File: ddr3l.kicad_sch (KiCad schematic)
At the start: 1 part

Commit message: write some things down
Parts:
- U1: renamed from U?; value MCIMX6YxxVMxxxx -> MCIMX6Y2DVM09AB; Manufacturer (none) -> NXP; MfgPartNo (none) -> MCIMX6Y2DVM09AB; Vendor (none) -> Digi-Key; VendorPartNo (none) -> 568-14995-ND
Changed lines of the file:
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@@
   (symbol (lib_id "catfood:MCIMX6YxxVMxxxx") (at 50.8 54.61 0) (unit 3)
     (in_bom yes) (on_board yes) (fields_autoplaced)
-    (property "Reference" "U?" (id 0) (at 50.8 24.13 0))
-    (property "Value" "MCIMX6YxxVMxxxx" (id 1) (at 50.8 26.67 0))
+    (property "Reference" "U1" (id 0) (at 50.8 24.13 0))
+    (property "Value" "MCIMX6Y2DVM09AB" (id 1) (at 50.8 26.67 0))
     (property "Footprint" "" (id 2) (at 40.64 35.56 0)
       (effects (font (size 1.27 1.27)) hide)
@@
       (effects (font (size 1.27 1.27)) hide)
     )
+    (property "Manufacturer" "NXP" (id 4) (at 50.8 34.29 0)
+      (effects (font (size 1.27 1.27)) hide)
+    )
+    (property "MfgPartNo" "MCIMX6Y2DVM09AB" (id 5) (at 50.8 36.83 0)
+      (effects (font (size 1.27 1.27)) hide)
+    )
+    (property "Vendor" "Digi-Key" (id 6) (at 50.8 39.37 0)
+      (effects (font (size 1.27 1.27)) hide)
+    )
+    (property "VendorPartNo" "568-14995-ND" (id 7) (at 50.8 41.91 0)
+      (effects (font (size 1.27 1.27)) hide)
+    )

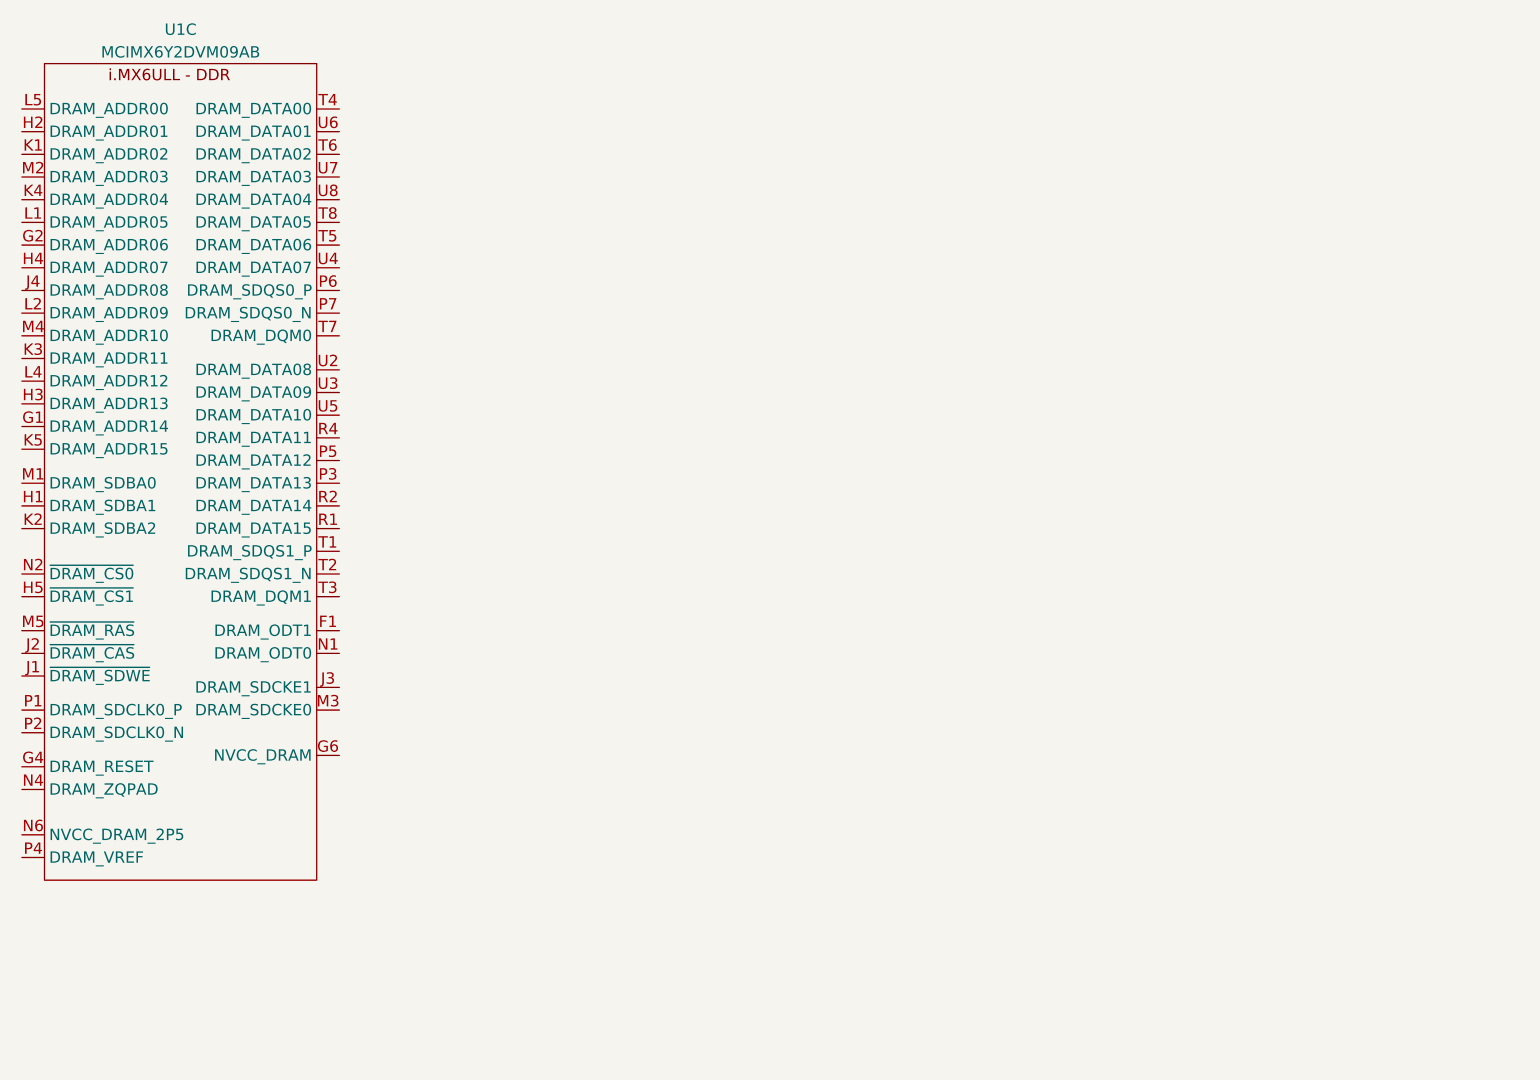
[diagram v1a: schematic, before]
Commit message: Added DDR3L symbol
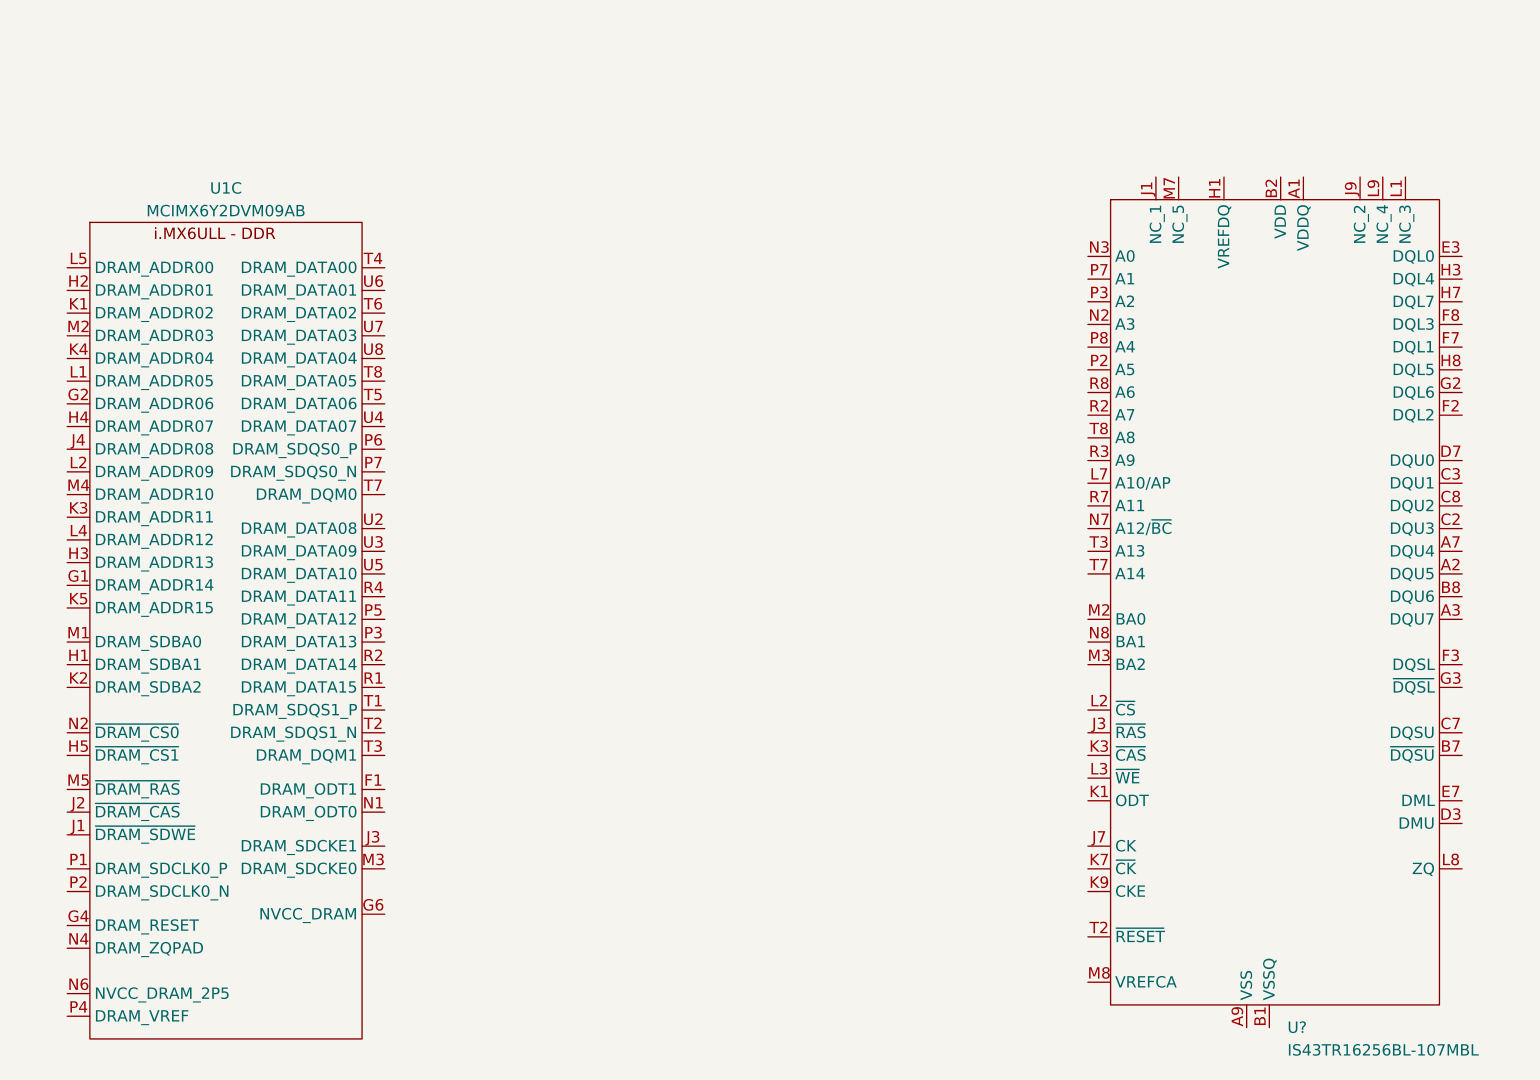
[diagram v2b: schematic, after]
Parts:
- added U?: IS43TR16256BL-107MBL, symbol catfood:IS43TR16256BL-107MBL
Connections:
- new net VDD: U?.B2 (VDD), U?.D9 (VDD), U?.G7 (VDD), U?.K2 (VDD), U?.K8 (VDD), U?.N1 (VDD), U?.N9 (VDD), U?.R1 (VDD), U?.R9 (VDD)
- new net VDDQ: U?.A1 (VDDQ), U?.A8 (VDDQ), U?.C1 (VDDQ), U?.C9 (VDDQ), U?.D2 (VDDQ), U?.E9 (VDDQ), U?.F1 (VDDQ), U?.H2 (VDDQ), U?.H9 (VDDQ)
- new net VSS: U?.A9 (VSS), U?.B3 (VSS), U?.E1 (VSS), U?.G8 (VSS), U?.J2 (VSS), U?.J8 (VSS), U?.M1 (VSS), U?.M9 (VSS), U?.P1 (VSS), U?.P9 (VSS), U?.T1 (VSS), U?.T9 (VSS)
- new net VSSQ: U?.B1 (VSSQ), U?.B9 (VSSQ), U?.D1 (VSSQ), U?.D8 (VSSQ), U?.E2 (VSSQ), U?.E8 (VSSQ), U?.F9 (VSSQ), U?.G1 (VSSQ), U?.G9 (VSSQ)
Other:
- moved on the sheet: U1C
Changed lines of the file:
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@@
     (company "Ian Kilgore")
   )
-  (symbol (lib_id "catfood:MCIMX6YxxVMxxxx") (at 50.8 54.61 0) (unit 3)
+  (symbol (lib_id "catfood:IS43TR16256BL-107MBL") (at 152.4 50.8 0) (unit 1)
     (in_bom yes) (on_board yes) (fields_autoplaced)
-    (property "Reference" "U1" (id 0) (at 50.8 24.13 0))
-    (property "Value" "MCIMX6Y2DVM09AB" (id 1) (at 50.8 26.67 0))
-    (property "Footprint" "" (id 2) (at 40.64 35.56 0)
+    (property "Reference" "U?" (id 0) (at 174.7394 135.89 0)
+      (effects (font (size 1.27 1.27)) (justify left))
+    )
+    (property "Value" "IS43TR16256BL-107MBL" (id 1) (at 174.7394 138.43 0)
+      (effects (font (size 1.27 1.27)) (justify left))
+    )
+    (property "Footprint" "" (id 2) (at 153.67 -1.27 0)
       (effects (font (size 1.27 1.27)) hide)
     )
-    (property "Datasheet" "" (id 3) (at 40.64 35.56 0)
+    (property "Datasheet" "" (id 3) (at 153.67 -1.27 0)
       (effects (font (size 1.27 1.27)) hide)
     )
-    (property "Manufacturer" "NXP" (id 4) (at 50.8 34.29 0)
+    (pin "A1")
+    (pin "A2")
+    (pin "A3")
+    (pin "A7")
+    (pin "A8")
+    (pin "A9")
+    (pin "B1")
+    (pin "B2")
+    (pin "B3")
+    (pin "B7")
+    (pin "B8")
+    (pin "B9")
+    (pin "C1")
+    (pin "C2")
+    (pin "C3")
+    (pin "C7")
+    (pin "C8")
+    (pin "C9")
+    (pin "D1")
+    (pin "D2")
+    (pin "D3")
+    (pin "D7")
+    (pin "D8")
+    (pin "D9")
+    (pin "E1")
+    (pin "E2")
+    (pin "E3")
+    (pin "E7")
+    (pin "E8")
+    (pin "E9")
+    (pin "F1")
+    (pin "F2")
+    (pin "F3")
+    (pin "F7")
+    (pin "F8")
+    (pin "F9")
+    (pin "G1")
+    (pin "G2")
+    (pin "G3")
+    (pin "G7")
+    (pin "G8")
+    (pin "G9")
+    (pin "H1")
+    (pin "H2")
+    (pin "H3")
+    (pin "H7")
+    (pin "H8")
+    (pin "H9")
+    (pin "J1")
+    (pin "J2")
+    (pin "J3")
+    (pin "J7")
+    (pin "J8")
+    (pin "J9")
+    (pin "K1")
+    (pin "K2")
+    (pin "K3")
+    (pin "K7")
+    (pin "K8")
+    (pin "K9")
+    (pin "L1")
+    (pin "L2")
+    (pin "L3")
+    (pin "L7")
+    (pin "L8")
+    (pin "L9")
+    (pin "M1")
+    (pin "M2")
+    (pin "M3")
+    (pin "M7")
+    (pin "M8")
+    (pin "M9")
+    (pin "N1")
+    (pin "N2")
+    (pin "N3")
+    (pin "N7")
+    (pin "N8")
+    (pin "N9")
+    (pin "P1")
+    (pin "P2")
+    (pin "P3")
+    (pin "P7")
+    (pin "P8")
+    (pin "P9")
+    (pin "R1")
+    (pin "R2")
+    (pin "R3")
+    (pin "R7")
+    (pin "R8")
+    (pin "R9")
+    (pin "T1")
+    (pin "T2")
+    (pin "T3")
+    (pin "T7")
+    (pin "T8")
+    (pin "T9")
+  )
+  (symbol (lib_id "catfood:MCIMX6YxxVMxxxx") (at 55.88 72.39 0) (unit 3)
+    (in_bom yes) (on_board yes) (fields_autoplaced)
+    (property "Reference" "U1" (id 0) (at 55.88 41.91 0))
+    (property "Value" "MCIMX6Y2DVM09AB" (id 1) (at 55.88 44.45 0))
+    (property "Footprint" "" (id 2) (at 45.72 53.34 0)
       (effects (font (size 1.27 1.27)) hide)
     )
-    (property "MfgPartNo" "MCIMX6Y2DVM09AB" (id 5) (at 50.8 36.83 0)
+    (property "Datasheet" "" (id 3) (at 45.72 53.34 0)
       (effects (font (size 1.27 1.27)) hide)
     )
-    (property "Vendor" "Digi-Key" (id 6) (at 50.8 39.37 0)
+    (property "Manufacturer" "NXP" (id 4) (at 55.88 52.07 0)
       (effects (font (size 1.27 1.27)) hide)
     )
-    (property "VendorPartNo" "568-14995-ND" (id 7) (at 50.8 41.91 0)
+    (property "MfgPartNo" "MCIMX6Y2DVM09AB" (id 5) (at 55.88 54.61 0)
       (effects (font (size 1.27 1.27)) hide)
     )
+    (property "Vendor" "Digi-Key" (id 6) (at 55.88 57.15 0)
+      (effects (font (size 1.27 1.27)) hide)
+    )
+    (property "VendorPartNo" "568-14995-ND" (id 7) (at 55.88 59.69 0)
+      (effects (font (size 1.27 1.27)) hide)
+    )

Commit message: DDR3L
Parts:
- added C? (x18): 0.22uF 0402, symbol Device:C_Small
- added C?: 4.7uF 0603, symbol Device:C_Small
- added C? (x2): 2.2pF 0402, symbol Device:C_Small
- added C? (x2): 0.1uF 0402, symbol Device:C_Small
- added C?: 10uF 0805, symbol Device:C_Small
- added R? (x3): 10k 0402, symbol Device:R_Small
- added R?: 470R 0402 1%, symbol Device:R_Small
- added R? (x2): 1.5k 0402 1%, symbol Device:R_Small
- added R? (x2): 240R 0402 1%, symbol Device:R_Small
- added R?: DNP 0402, symbol Device:R_Small
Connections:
- net VSSQ is gone; now on net GND: U?.B1 (VSSQ), U?.B9 (VSSQ), U?.D1 (VSSQ), U?.D8 (VSSQ), U?.E2 (VSSQ), U?.E8 (VSSQ), U?.F9 (VSSQ), U?.G1 (VSSQ), U?.G9 (VSSQ)
- net DRAM_DATA13: now reaches U?.A2 (DQU5)
- net DRAM_DATA13: now also U1.P3 (DRAM_DATA13)
- net DRAM_DATA15: now reaches U?.A3 (DQU7)
- net DRAM_DATA15: now also U1.R1 (DRAM_DATA15)
- net DRAM_DATA12: now reaches U?.A7 (DQU4)
- net DRAM_DATA12: now also U1.P5 (DRAM_DATA12)
- net DRAM_SDQS1_N: now reaches U?.B7 (~{DQSU})
- net DRAM_SDQS1_N: now also U1.T2 (DRAM_SDQS1_N), C?.2
- net DRAM_DATA14: now reaches U?.B8 (DQU6)
- net DRAM_DATA14: now also U1.R2 (DRAM_DATA14)
- net DRAM_DATA11: now reaches U?.C2 (DQU3)
- net DRAM_DATA11: now also U1.R4 (DRAM_DATA11)
- net DRAM_DATA9: now reaches U?.C3 (DQU1)
- net DRAM_DATA9: now also U1.U3 (DRAM_DATA09)
- net DRAM_SDQS1_P: now reaches U?.C7 (DQSU)
- net DRAM_SDQS1_P: now also U1.T1 (DRAM_SDQS1_P), C?.1
- net DRAM_DATA10: now reaches U?.C8 (DQU2)
- net DRAM_DATA10: now also U1.U5 (DRAM_DATA10)
- net DRAM_DQM1: now reaches U?.D3 (DMU)
- net DRAM_DQM1: now also U1.T3 (DRAM_DQM1)
- net DRAM_DATA8: now reaches U?.D7 (DQU0)
- net DRAM_DATA8: now also U1.U2 (DRAM_DATA08)
- net DRAM_DATA0: now reaches U?.E3 (DQL0)
- net DRAM_DATA0: now also U1.T4 (DRAM_DATA00)
- net DRAM_DQM0: now reaches U?.E7 (DML)
- net DRAM_DQM0: now also U1.T7 (DRAM_DQM0)
- net DRAM_DATA7: now reaches U?.F2 (DQL2)
- net DRAM_DATA7: now also U1.U4 (DRAM_DATA07)
- net DRAM_SDQS0_P: now reaches U?.F3 (DQSL)
- net DRAM_SDQS0_P: now also U1.P6 (DRAM_SDQS0_P), C?.1
- net DRAM_DATA4: now reaches U?.F7 (DQL1)
- net DRAM_DATA4: now also U1.U8 (DRAM_DATA04)
- net DRAM_DATA3: now reaches U?.F8 (DQL3)
- net DRAM_DATA3: now also U1.U7 (DRAM_DATA03)
- net DRAM_DATA6: now reaches U?.G2 (DQL6)
- net DRAM_DATA6: now also U1.T5 (DRAM_DATA06)
- net DRAM_SDQS0_N: now reaches U?.G3 (~{DQSL})
- net DRAM_SDQS0_N: now also U1.P7 (DRAM_SDQS0_N), C?.2
- net DRAM_VREF: now reaches U?.H1 (VREFDQ)
- net DRAM_VREF: now also U1.P4 (DRAM_VREF), U?.M8 (VREFCA), C?.1, C?.1, C?.1, C?.1, C?.2, R?.1, R?.2
- net DRAM_DATA1: now reaches U?.H3 (DQL4)
- net DRAM_DATA1: now also U1.U6 (DRAM_DATA01)
- net DRAM_DATA2: now reaches U?.H7 (DQL7)
- net DRAM_DATA2: now also U1.T6 (DRAM_DATA02)
- net DRAM_DATA5: now reaches U?.H8 (DQL5)
- net DRAM_DATA5: now also U1.T8 (DRAM_DATA05)
- net DRAM_ODT1: now reaches U?.J1 (NC_1)
- net DRAM_ODT1: now also U1.F1 (DRAM_ODT1)
- net DRAM_RAS_B: now reaches U?.J3 (~{RAS})
- net DRAM_RAS_B: now also U1.M5 (~{DRAM_RAS})
- net DRAM_SDCLK0_P: now reaches U?.J7 (CK)
- net DRAM_SDCLK0_P: now also U1.P1 (DRAM_SDCLK0_P), R?.1
- net DRAM_SDCKE1: now reaches U?.J9 (NC_2)
- net DRAM_SDCKE1: now also U1.J3 (DRAM_SDCKE1), R?.1
- net DRAM_ODT0: now reaches U?.K1 (ODT)
- net DRAM_ODT0: now also U1.N1 (DRAM_ODT0)
- net DRAM_CAS_B: now reaches U?.K3 (~{CAS})
- net DRAM_CAS_B: now also U1.J2 (~{DRAM_CAS})
- net DRAM_SDCLK0_N: now reaches U?.K7 (~{CK})
- net DRAM_SDCLK0_N: now also U1.P2 (DRAM_SDCLK0_N), R?.2
- net DRAM_SDCKE0: now reaches U?.K9 (CKE)
- net DRAM_SDCKE0: now also U1.M3 (DRAM_SDCKE0), R?.1
- net DRAM_CS1_B: now reaches U?.L1 (NC_3)
- net DRAM_CS1_B: now also U1.H5 (~{DRAM_CS1})
- net DRAM_CS0_B: now reaches U?.L2 (~{CS})
- net DRAM_CS0_B: now also U1.N2 (~{DRAM_CS0})
- net DRAM_SDWE_B: now reaches U?.L3 (~{WE})
- net DRAM_SDWE_B: now also U1.J1 (~{DRAM_SDWE})
- net DRAM_ADDR10: now reaches U?.L7 (A10/AP)
- net DRAM_ADDR10: now also U1.M4 (DRAM_ADDR10)
- net DRAM_ZQ0: now reaches U?.L8 (ZQ)
- net DRAM_ZQ0: now also R?.1
- net DRAM_ZQ1: now reaches U?.L9 (NC_4)
- net DRAM_ZQ1: now also R?.1
- net DRAM_SDBA0: now reaches U?.M2 (BA0)
- net DRAM_SDBA0: now also U1.M1 (DRAM_SDBA0)
- net DRAM_SDBA2: now reaches U?.M3 (BA2)
- net DRAM_SDBA2: now also U1.K2 (DRAM_SDBA2)
- net DRAM_ADDR15: now reaches U?.M7 (NC_5)
- net DRAM_ADDR15: now also U1.K5 (DRAM_ADDR15)
- net DRAM_ADDR3: now reaches U?.N2 (A3)
- net DRAM_ADDR3: now also U1.M2 (DRAM_ADDR03)
- net DRAM_ADDR0: now reaches U?.N3 (A0)
- net DRAM_ADDR0: now also U1.L5 (DRAM_ADDR00)
- net DRAM_ADDR12: now reaches U?.N7 (A12/~{BC})
- net DRAM_ADDR12: now also U1.L4 (DRAM_ADDR12)
- net DRAM_SDBA1: now reaches U?.N8 (BA1)
- net DRAM_SDBA1: now also U1.H1 (DRAM_SDBA1)
- net DRAM_ADDR5: now reaches U?.P2 (A5)
- net DRAM_ADDR5: now also U1.L1 (DRAM_ADDR05)
- net DRAM_ADDR2: now reaches U?.P3 (A2)
- net DRAM_ADDR2: now also U1.K1 (DRAM_ADDR02)
- net DRAM_ADDR1: now reaches U?.P7 (A1)
- net DRAM_ADDR1: now also U1.H2 (DRAM_ADDR01)
- net DRAM_ADDR4: now reaches U?.P8 (A4)
- net DRAM_ADDR4: now also U1.K4 (DRAM_ADDR04)
- net DRAM_ADDR7: now reaches U?.R2 (A7)
- net DRAM_ADDR7: now also U1.H4 (DRAM_ADDR07)
- net DRAM_ADDR9: now reaches U?.R3 (A9)
- net DRAM_ADDR9: now also U1.L2 (DRAM_ADDR09)
- net DRAM_ADDR11: now reaches U?.R7 (A11)
- net DRAM_ADDR11: now also U1.K3 (DRAM_ADDR11)
- net DRAM_ADDR6: now reaches U?.R8 (A6)
- net DRAM_ADDR6: now also U1.G2 (DRAM_ADDR06)
- net DRAM_RESET_B: now reaches U?.T2 (~{RESET})
- net DRAM_RESET_B: now also U1.G4 (DRAM_RESET), R?.1
- net DRAM_ADDR13: now reaches U?.T3 (A13)
- net DRAM_ADDR13: now also U1.H3 (DRAM_ADDR13)
- net DRAM_ADDR14: now reaches U?.T7 (A14)
- net DRAM_ADDR14: now also U1.G1 (DRAM_ADDR14)
- net DRAM_ADDR8: now reaches U?.T8 (A8)
- net DRAM_ADDR8: now also U1.J4 (DRAM_ADDR08)
- net VDD_1V35: now reaches U1.G6 (NVCC_DRAM), U1.H6 (NVCC_DRAM), U1.J6 (NVCC_DRAM), U1.K6 (NVCC_DRAM), U1.L6 (NVCC_DRAM), U1.M6 (NVCC_DRAM)
- net VDD_1V35: now also C?.1, C?.1, C?.1, C?.1, C?.1, C?.1, C?.1, C?.1, C?.1, C?.1, C?.1, C?.1, C?.1, C?.1, C?.1, C?.1, C?.1, R?.1
- net DRAM_ZQPAD: now reaches U1.N4 (DRAM_ZQPAD)
- net DRAM_ZQPAD: now also R?.2
- net VDD_HIGH_CAP: now reaches U1.N6 (NVCC_DRAM_2P5)
- net VDD_HIGH_CAP: now also C?.1
- net VSS renamed GND
- net GND: now also C?.2, C?.2, C?.2, C?.2, C?.2, C?.2, C?.2, C?.2, C?.2, C?.2, C?.2, C?.2, C?.2, C?.2, C?.2, C?.2, C?.2, C?.2, C?.2, C?.2, C?.2, R?.1, R?.2, R?.2, R?.2, R?.2, R?.2, R?.2
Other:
- note added: "512MiB, 16-bit"
- moved on the sheet: U1C, U?

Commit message: Annotation
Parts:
- gave numbers to parts that had none: 34
- renumbered U1 to U4
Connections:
- net VDDQ is gone; now on net VDD: U6.A1 (VDDQ), U6.A8 (VDDQ), U6.C1 (VDDQ), U6.C9 (VDDQ), U6.D2 (VDDQ), U6.E9 (VDDQ), U6.F1 (VDDQ), U6.H2 (VDDQ), U6.H9 (VDDQ)
- net VDD_1V35 is gone; now on net VDD: C45.1, C46.1, C47.1, C48.1, C51.1, C52.1, C53.1, C54.1, C57.1, C59.1, C60.1, C61.1, C62.1, C63.1, C64.1, C65.1, C66.1, R18.1, U4.G6 (NVCC_DRAM), U4.H6 (NVCC_DRAM), U4.J6 (NVCC_DRAM), U4.K6 (NVCC_DRAM), U4.L6 (NVCC_DRAM), U4.M6 (NVCC_DRAM)
